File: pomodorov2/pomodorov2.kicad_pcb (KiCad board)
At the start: 2 copper layers, 56.9 x 38.4 mm, 5 parts, among them J1 Conn_ARM_JTAG_SWD_10, J2 TC2050-IDC, J3 Conn_01x08, U1 nRF52832-QFxx

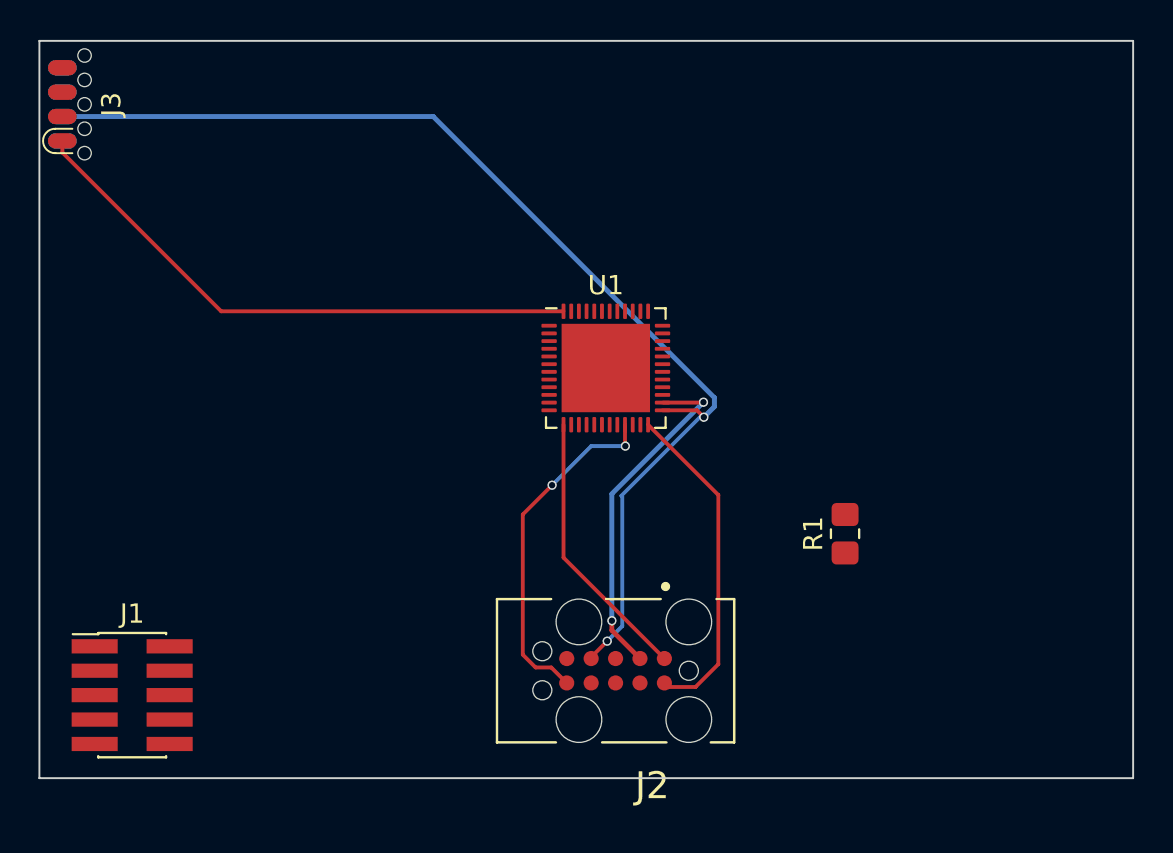
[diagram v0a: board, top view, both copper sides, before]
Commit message: Remove cortex header
- remove main cortex header
- tag-connect remains
- soicbite remains
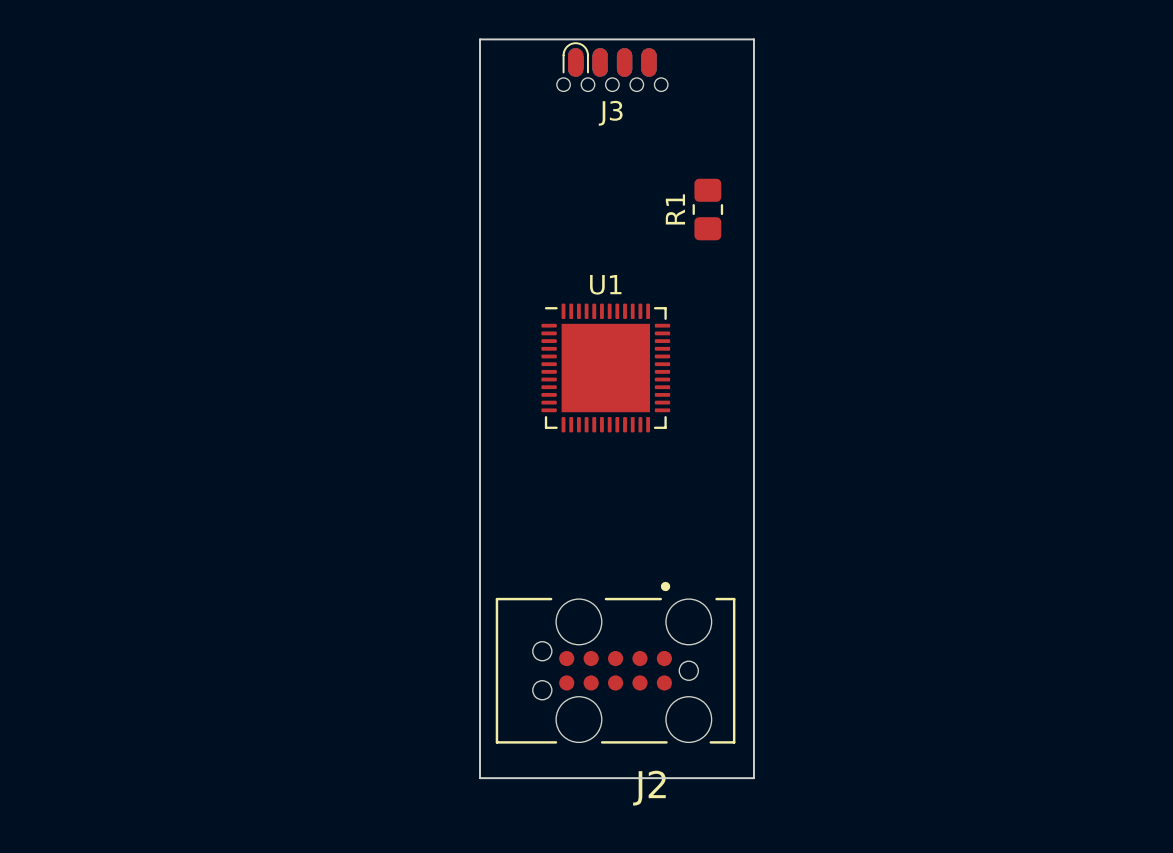
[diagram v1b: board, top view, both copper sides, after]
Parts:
- removed J1: Conn_ARM_JTAG_SWD_10, Connector_PinHeader_1.27mm:PinHeader_2x05_P1.27mm_Vertical_SMD
- moved J3 29.5 mm to (156.0, 105.5), turned to 180 degrees
- moved R1 18.3 mm to (161.0, 113.9)
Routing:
- net SWCLK: track 58.7 -> 0.07 mm, vias 2 -> 0
- net VCC: track 44.4 -> 0.00 mm
- net SWO: track 18.1 -> 0.00 mm, vias 2 -> 0
- net SWDIO: track 18.2 -> 0.13 mm, vias 2 -> 0
- net ~RESET: track 17.4 -> 0.30 mm
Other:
- board size 56.9 x 38.4 mm -> 14.3 x 38.4 mm

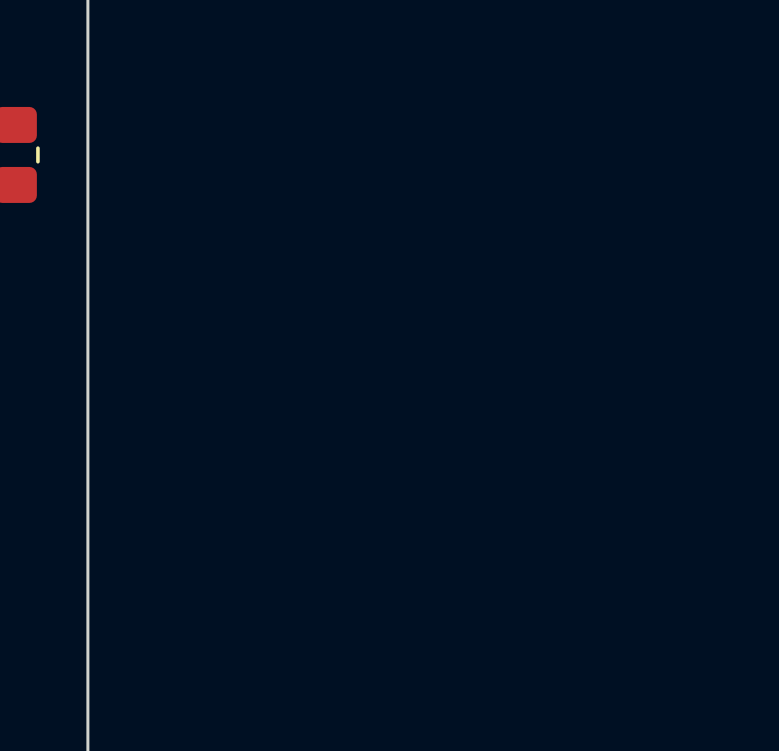
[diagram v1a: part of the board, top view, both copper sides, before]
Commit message: Add components for chip, no routing 🚏
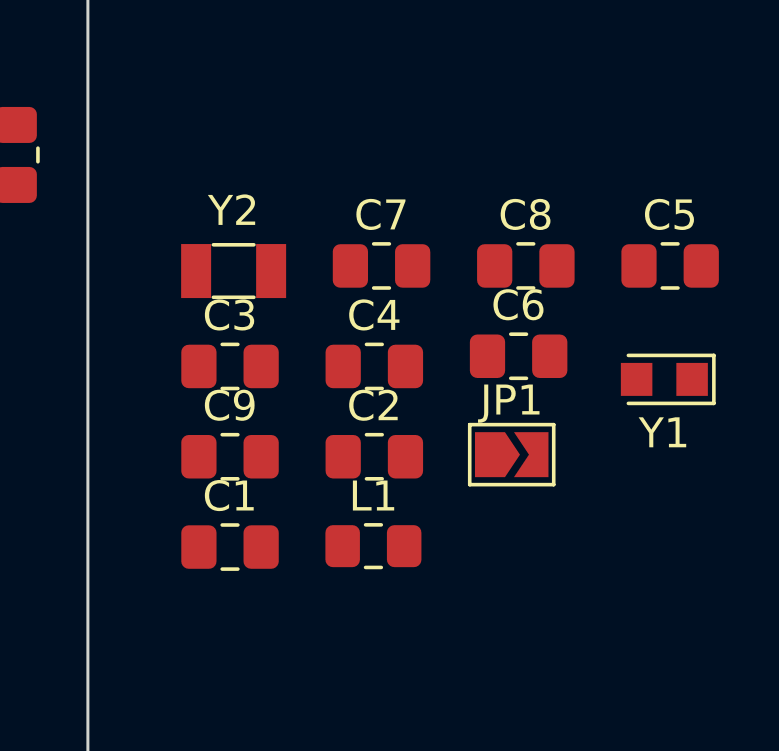
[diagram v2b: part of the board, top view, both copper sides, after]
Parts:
- added C1: 12pF, Capacitor_SMD:C_0805_2012Metric_Pad1.18x1.45mm_HandSolder, F.Cu at (168.1, 127.0)
- added C2: 12pF, Capacitor_SMD:C_0805_2012Metric_Pad1.18x1.45mm_HandSolder, F.Cu at (173.0, 124.0)
- added C3: 0.8pF, Capacitor_SMD:C_0805_2012Metric_Pad1.18x1.45mm_HandSolder, F.Cu at (168.1, 121.0)
- added C4: 100nF, Capacitor_SMD:C_0805_2012Metric_Pad1.18x1.45mm_HandSolder, F.Cu at (173.0, 121.0)
- added C5: 100pF, Capacitor_SMD:C_0805_2012Metric_Pad1.18x1.45mm_HandSolder, F.Cu at (182.8, 117.6)
- added C6: 1.0uF, Capacitor_SMD:C_0805_2012Metric_Pad1.18x1.45mm_HandSolder, F.Cu at (177.8, 120.6)
- added C7: 100nF, Capacitor_SMD:C_0805_2012Metric_Pad1.18x1.45mm_HandSolder, F.Cu at (173.2, 117.6)
- added C8: 12pF, Capacitor_SMD:C_0805_2012Metric_Pad1.18x1.45mm_HandSolder, F.Cu at (178.0, 117.6)
- added C9: 12pF, Capacitor_SMD:C_0805_2012Metric_Pad1.18x1.45mm_HandSolder, F.Cu at (168.1, 124.0)
- added JP1: SolderJumper_2_Open, Jumper:SolderJumper-2_P1.3mm_Open_TrianglePad1.0x1.5mm, F.Cu at (177.5, 123.9)
- added L1: 3.9nH, Inductor_SMD:L_0805_2012Metric_Pad1.15x1.40mm_HandSolder, F.Cu at (172.9, 127.0)
- added Y1: 32MHz, Crystal:Crystal_SMD_2012-2Pin_2.0x1.2mm_HandSoldering, F.Cu at (182.6, 121.4)
- added Y2: 32.768kHz, Crystal:Crystal_SMD_3215-2Pin_3.2x1.5mm, F.Cu at (168.3, 117.8)
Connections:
- R1 pad 1: VCC -> SWDIO
- R1 pad 2: SWDIO -> VCC
- U1 pad 1: unconnected-(U1-Pad1) -> Net-(U1-Pad1)
- U1 pad 13: VCC -> VDD
- U1 pad 2: unconnected-(U1-Pad2) -> Net-(U1-Pad2)
- U1 pad 3: unconnected-(U1-Pad3) -> Net-(U1-Pad3)
- U1 pad 30: unconnected-(U1-Pad30) -> Net-(U1-Pad30)
- U1 pad 31: Net-(U1-Pad31) -> GND
- U1 pad 32: unconnected-(U1-Pad32) -> Net-(U1-Pad32)
- U1 pad 33: unconnected-(U1-Pad33) -> Net-(U1-Pad33)
- U1 pad 34: unconnected-(U1-Pad34) -> Net-(U1-Pad34)
- U1 pad 35: unconnected-(U1-Pad35) -> Net-(U1-Pad35)
- U1 pad 36: VCC -> VDD
- U1 pad 45: Net-(U1-Pad31) -> GND
- U1 pad 46: unconnected-(U1-Pad46) -> Net-(U1-Pad46)
- U1 pad 48: VCC -> VDD
- U1 pad 49: Net-(U1-Pad31) -> GND

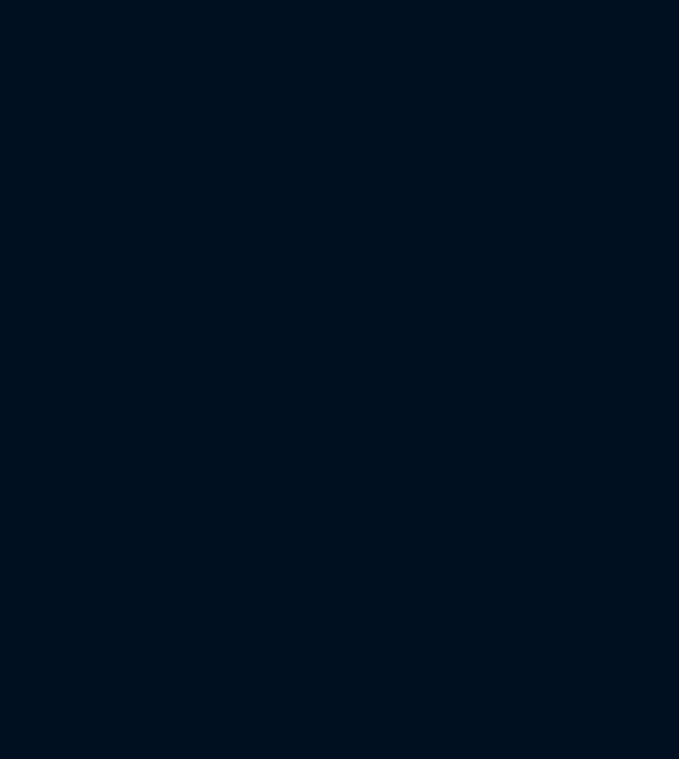
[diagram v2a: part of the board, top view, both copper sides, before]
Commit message: Add Adafruit MDBT50Q-1MV2, remove nRF52832 QFN 🔄
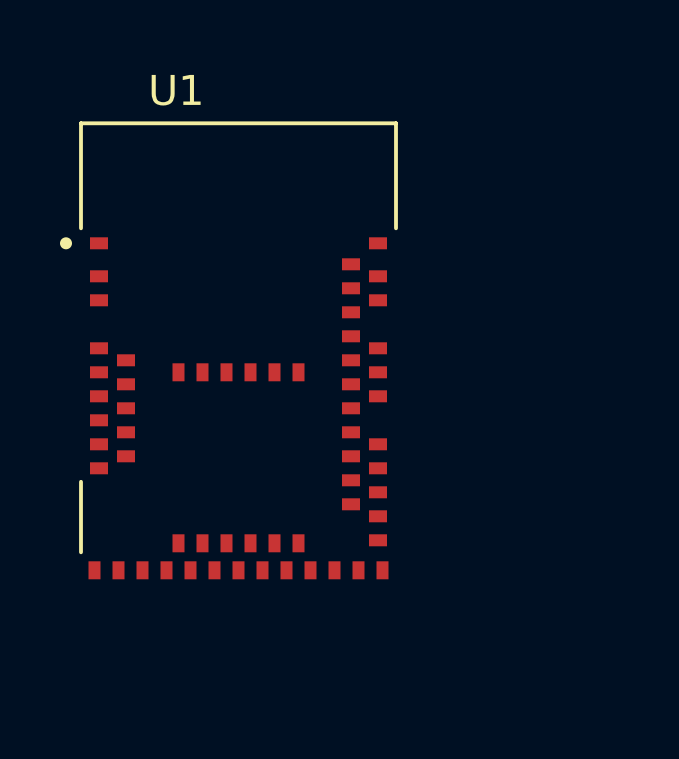
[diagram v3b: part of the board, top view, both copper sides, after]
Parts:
- added U1: MDBT50Q-1MV2, MDBT50Q-1MV2:XCVR_MDBT50Q-1MV2, F.Cu at (125.7, 99.8)

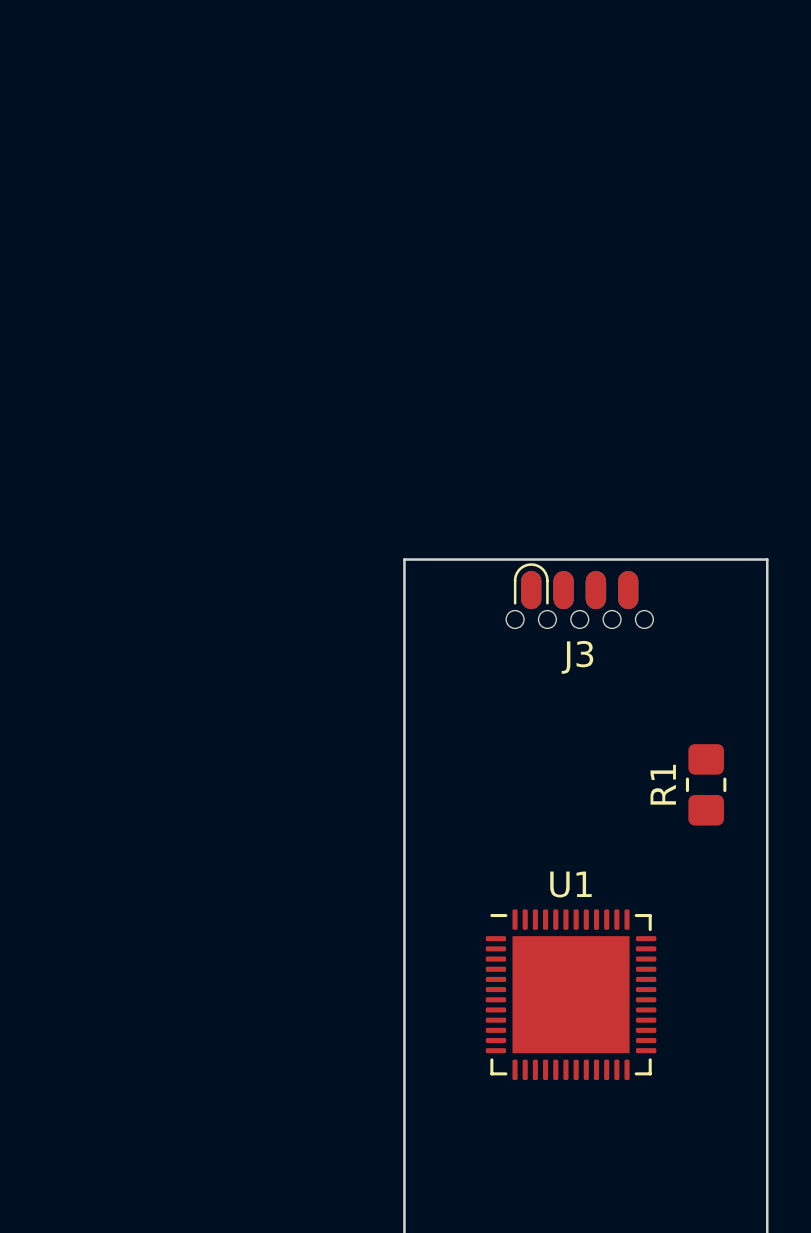
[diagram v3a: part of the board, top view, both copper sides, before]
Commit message: Adding test points, usb, crystals 💎
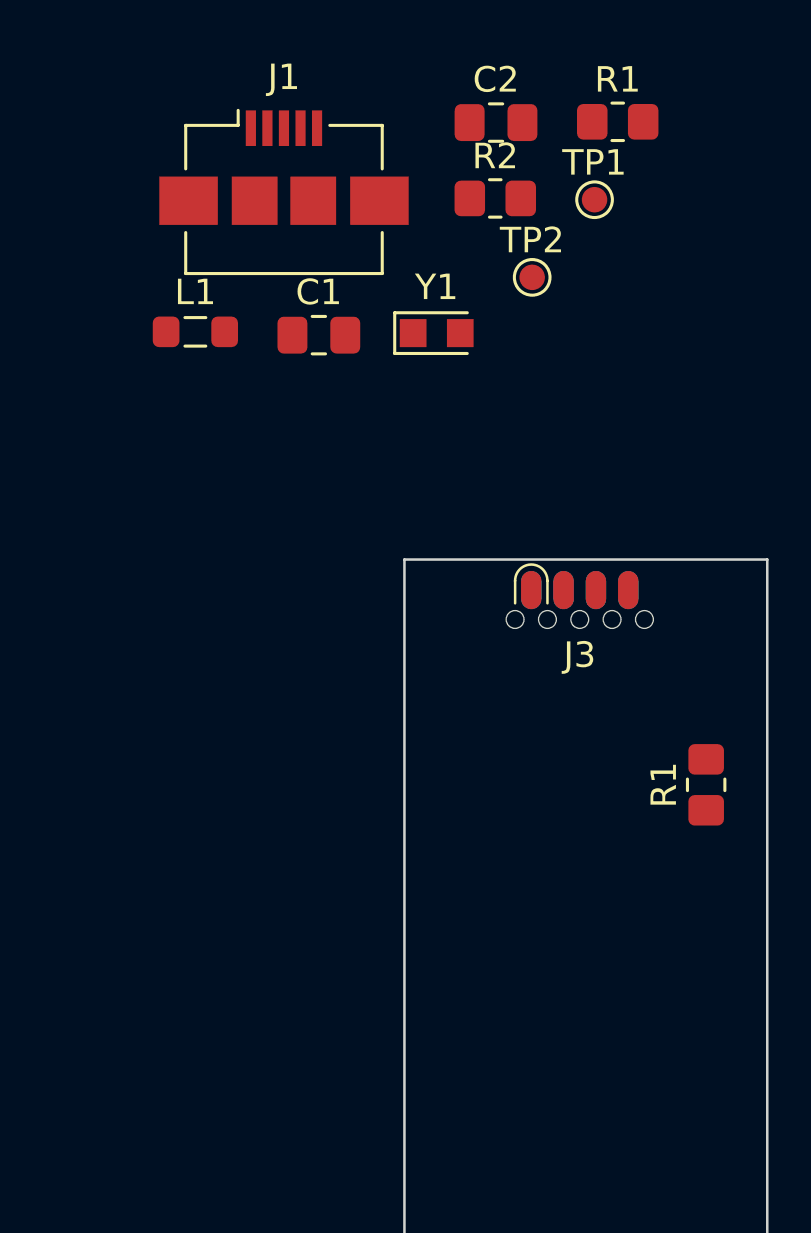
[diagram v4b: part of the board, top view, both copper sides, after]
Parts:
- removed the U1 at (155.7, 122.2)
- added C1: 22pF, Capacitor_SMD:C_0805_2012Metric_Pad1.18x1.45mm_HandSolder, F.Cu at (145.8, 96.3)
- added C2: 22pF, Capacitor_SMD:C_0805_2012Metric_Pad1.18x1.45mm_HandSolder, F.Cu at (152.8, 87.9)
- added J1: USB_B_Micro, Connector_USB:USB_Micro-B_Amphenol_10104110_Horizontal, F.Cu at (144.4, 89.7)
- added L1: 10uH (DNP?), Inductor_SMD:L_0805_2012Metric_Pad1.05x1.20mm_HandSolder, F.Cu at (140.9, 96.1)
- added R1: 22, Resistor_SMD:R_0805_2012Metric_Pad1.20x1.40mm_HandSolder, F.Cu at (157.5, 87.9)
- added R2: 22, Resistor_SMD:R_0805_2012Metric_Pad1.20x1.40mm_HandSolder, F.Cu at (152.7, 90.9)
- added TP1: TestPoint, TestPoint:TestPoint_Pad_D1.0mm, F.Cu at (156.6, 90.9)
- added TP2: TestPoint, TestPoint:TestPoint_Pad_D1.0mm, F.Cu at (154.2, 94.0)
- added Y1: 32.768kHz, Crystal:Crystal_SMD_2012-2Pin_2.0x1.2mm_HandSoldering, F.Cu at (150.4, 96.2)
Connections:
- U1 pad 1: Net-(U1-Pad1) -> GND
- U1 pad 15: Net-(U1-Pad1) -> GND
- U1 pad 17: unconnected-(U1-Pad17) -> Net-(U1-Pad17)
- U1 pad 18: unconnected-(U1-Pad18) -> Net-(U1-Pad18)
- U1 pad 2: Net-(U1-Pad1) -> GND
- U1 pad 28: unconnected-(U1-Pad28) -> VCC
- U1 pad 30: unconnected-(U1-Pad30) -> VCC
- U1 pad 31: unconnected-(U1-Pad31) -> Net-(U1-Pad31)
- U1 pad 33: Net-(U1-Pad1) -> GND
- U1 pad 51: unconnected-(U1-Pad51) -> SWDIO
- U1 pad 53: unconnected-(U1-Pad53) -> SWCLK
- U1 pad 55: Net-(U1-Pad1) -> GND
